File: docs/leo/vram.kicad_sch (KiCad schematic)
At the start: 2 parts, among them IC25 UPD43256AC-10L, IC26 UPD43256AC-10L

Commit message: Add more b board logic
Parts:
- added IC23, IC24: 74LS273, symbol 74xx:74LS273
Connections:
- net VRAM_D0: now also IC24.18 (D7)
- net VRAM_D1: now also IC24.17 (D6)
- net VRAM_D10: now also IC23.14 (D5)
- net VRAM_D11: now also IC23.13 (D4)
- net VRAM_D12: now also IC23.8 (D3)
- net VRAM_D13: now also IC23.7 (D2)
- net VRAM_D14: now also IC23.4 (D1)
- net VRAM_D15: now also IC23.3 (D0)
- net VRAM_D2: now also IC24.14 (D5)
- net VRAM_D3: now also IC24.13 (D4)
- net VRAM_D4: now also IC24.8 (D3)
- net VRAM_D5: now also IC24.7 (D2)
- net VRAM_D6: now also IC24.4 (D1)
- net VRAM_D7: now also IC24.3 (D0)
- net VRAM_D8: now also IC23.18 (D7)
- net VRAM_D9: now also IC23.17 (D6)
- new net PA10: IC23.2 (Q0)
- new net PA11: IC24.19 (Q7)
- new net PA12: IC24.16 (Q6)
- new net PA13: IC24.15 (Q5)
- new net PA14: IC24.12 (Q4)
- new net PA15: IC24.9 (Q3)
- new net PA16: IC24.6 (Q2)
- new net PA17: IC24.5 (Q1)
- new net PA18: IC24.2 (Q0)
- new net PA3: IC23.19 (Q7)
- new net PA4: IC23.16 (Q6)
- new net PA5: IC23.15 (Q5)
- new net PA6: IC23.12 (Q4)
- new net PA7: IC23.9 (Q3)
- new net PA8: IC23.6 (Q2)
- new net PA9: IC23.5 (Q1)
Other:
- moved on the sheet: IC25, IC26

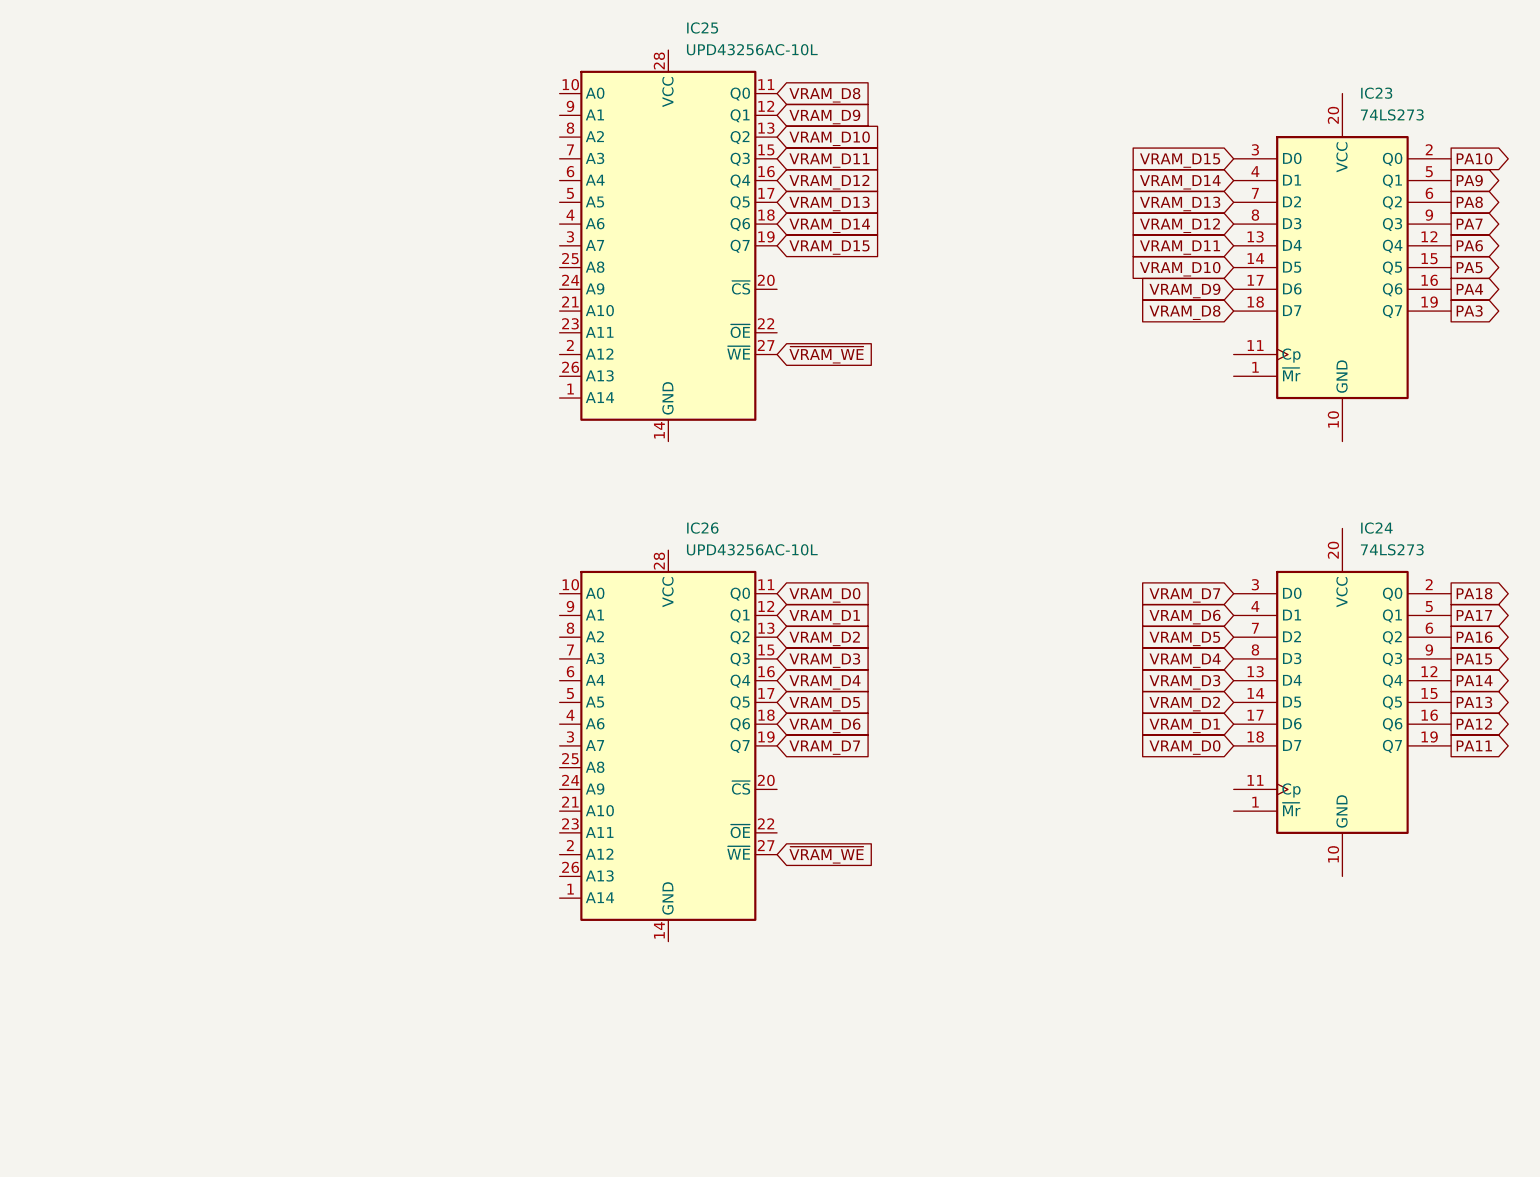
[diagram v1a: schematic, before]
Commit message: Decode M92-B-7H-D PAL
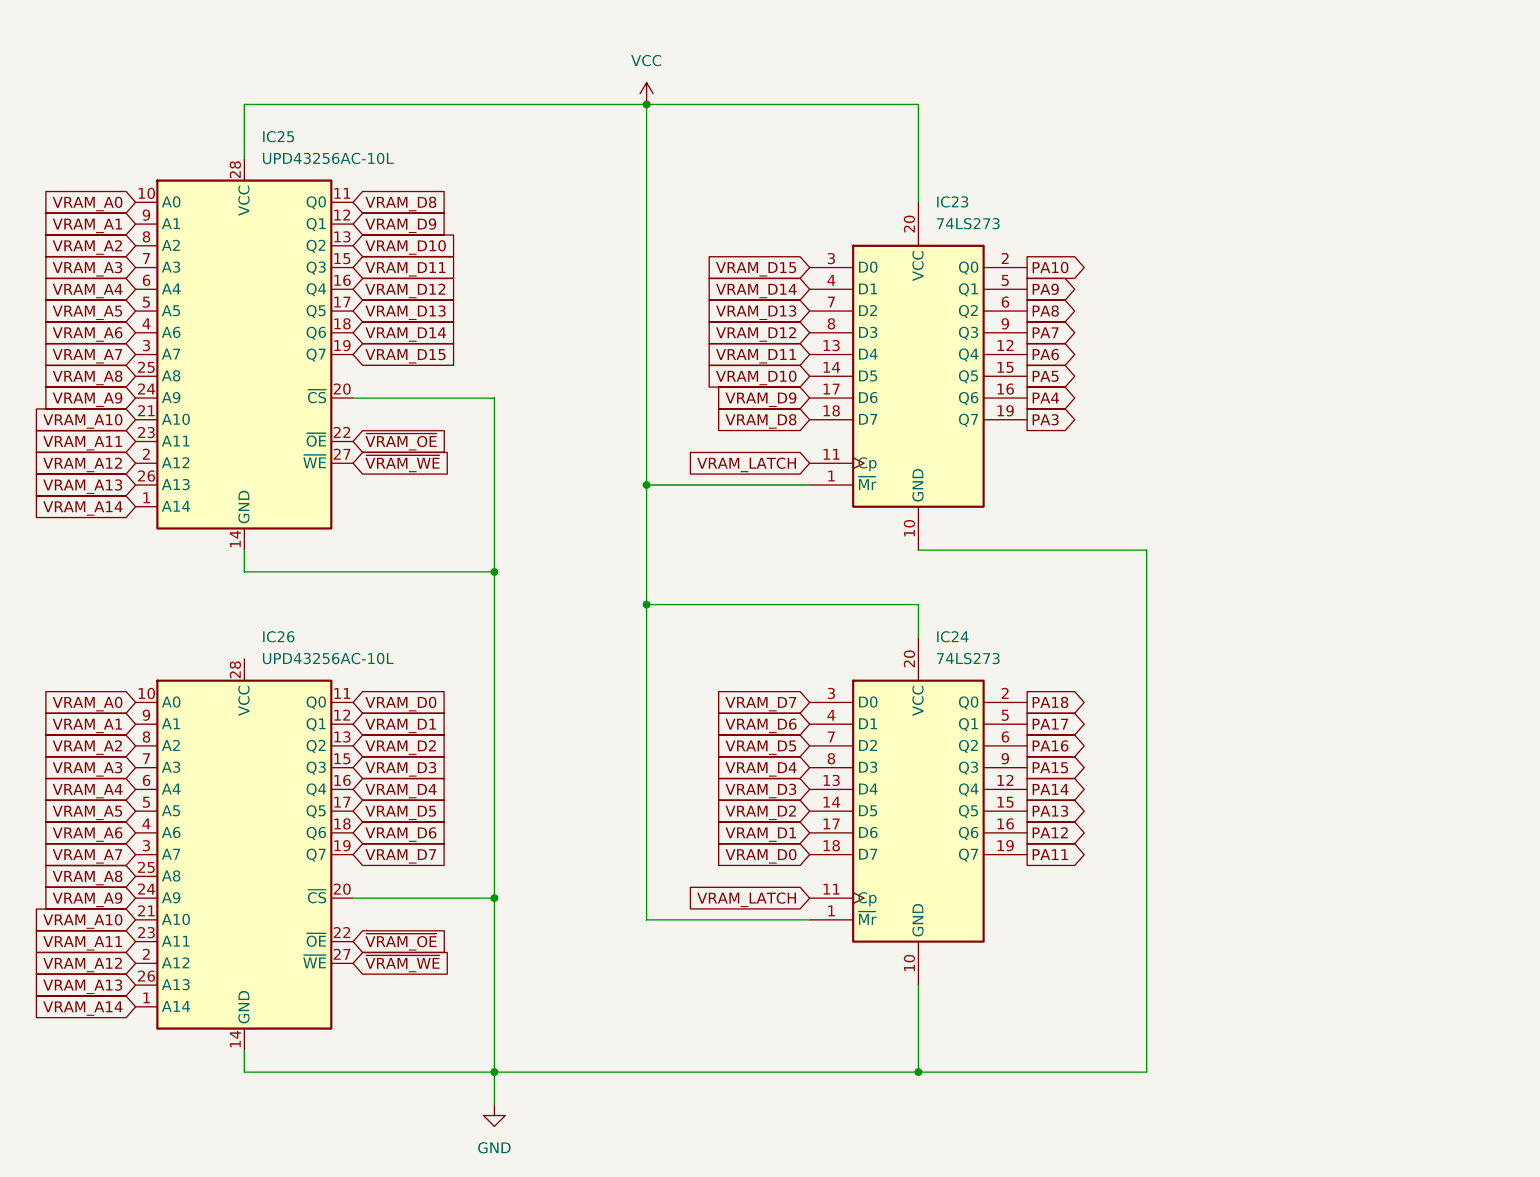
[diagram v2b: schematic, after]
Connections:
- net VRAM_A14: now reaches IC25.1 (A14)
- net VRAM_A14: now also IC26.1 (A14)
- net VRAM_A0: now reaches IC25.10 (A0)
- net VRAM_A0: now also IC26.10 (A0)
- net GND: now reaches IC25.14 (GND)
- net GND: now also IC23.10 (GND), IC24.10 (GND), IC25.20 (~{CS}), IC26.14 (GND), IC26.20 (~{CS})
- net VRAM_A12: now reaches IC25.2 (A12)
- net VRAM_A12: now also IC26.2 (A12)
- net VRAM_A10: now reaches IC25.21 (A10)
- net VRAM_A10: now also IC26.21 (A10)
- net ~{VRAM_OE}: now reaches IC25.22 (~{OE})
- net ~{VRAM_OE}: now also IC26.22 (~{OE})
- net VRAM_A11: now reaches IC25.23 (A11)
- net VRAM_A11: now also IC26.23 (A11)
- net VRAM_A9: now reaches IC25.24 (A9)
- net VRAM_A9: now also IC26.24 (A9)
- net VRAM_A8: now reaches IC25.25 (A8)
- net VRAM_A8: now also IC26.25 (A8)
- net VRAM_A13: now reaches IC25.26 (A13)
- net VRAM_A13: now also IC26.26 (A13)
- net VCC: now reaches IC25.28 (VCC)
- net VCC: now also IC23.1 (~{Mr}), IC23.20 (VCC), IC24.1 (~{Mr}), IC24.20 (VCC)
- net VRAM_A7: now reaches IC25.3 (A7)
- net VRAM_A7: now also IC26.3 (A7)
- net VRAM_A6: now reaches IC25.4 (A6)
- net VRAM_A6: now also IC26.4 (A6)
- net VRAM_A5: now reaches IC25.5 (A5)
- net VRAM_A5: now also IC26.5 (A5)
- net VRAM_A4: now reaches IC25.6 (A4)
- net VRAM_A4: now also IC26.6 (A4)
- net VRAM_A3: now reaches IC25.7 (A3)
- net VRAM_A3: now also IC26.7 (A3)
- net VRAM_A2: now reaches IC25.8 (A2)
- net VRAM_A2: now also IC26.8 (A2)
- net VRAM_A1: now reaches IC25.9 (A1)
- net VRAM_A1: now also IC26.9 (A1)
- net VRAM_LATCH: now reaches IC23.11 (Cp)
- net VRAM_LATCH: now also IC24.11 (Cp)
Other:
- moved on the sheet: IC23, IC24, IC25, IC26
